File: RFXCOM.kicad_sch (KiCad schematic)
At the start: 5 parts

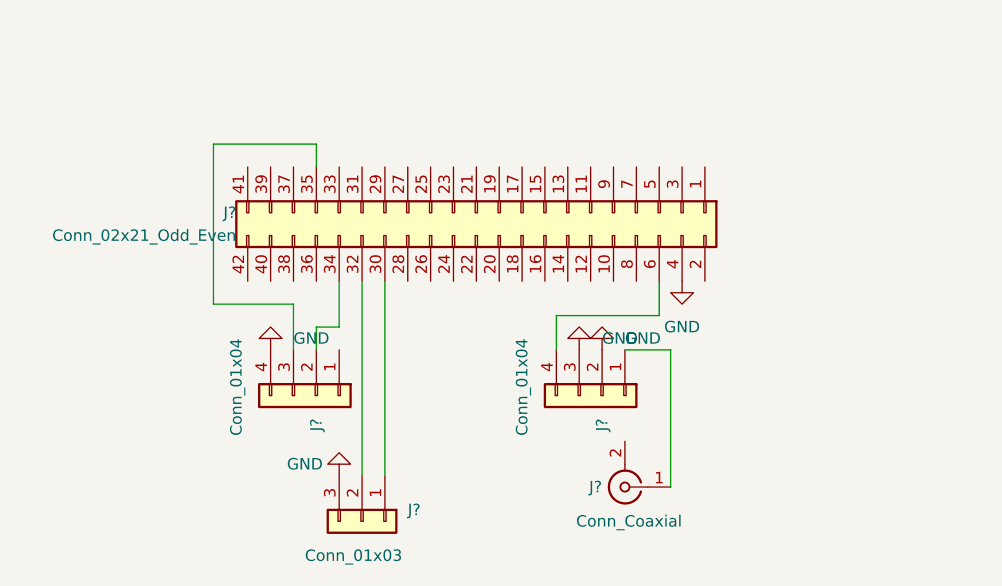
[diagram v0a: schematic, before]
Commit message: Rework the schematics a bit with labels. Add a RXB6 footprint. Also add a .gitignore
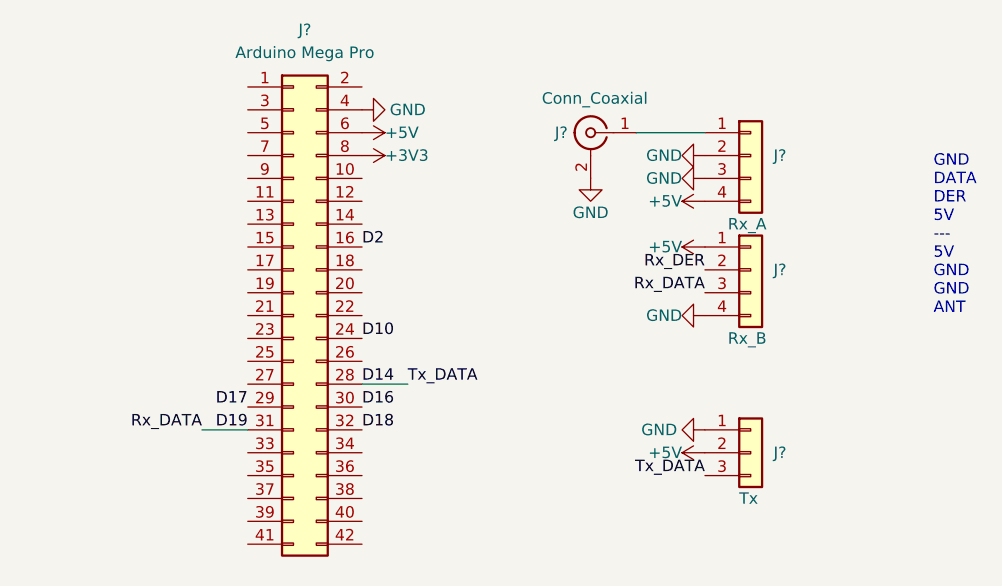
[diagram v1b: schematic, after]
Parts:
- removed J?: Conn_01x04, symbol Connector_Generic:Conn_01x04
- added J?: Rx_B, symbol Connector_Generic:Conn_01x04
- J?: value Conn_01x04 -> Rx_A
- J?: value Conn_01x03 -> Tx
- J?: value Conn_02x21_Odd_Even -> Arduino Mega Pro
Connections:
- net GND: now also J?.1 (Pin_1), J?.2 (Ext), J?.4 (Pin_4); no longer J?.3 (Pin_3)
- net +5V: now reaches J?.4 (Pin_4), J?.6 (Pin_6)
- net +5V: now also J?.2 (Pin_2), J?.1 (Pin_1)
- net D16: now reaches J?.30 (Pin_30)
- net D16: no longer J?.1 (Pin_1)
- net D18: now reaches J?.32 (Pin_32)
- net D18: no longer J?.2 (Pin_2)
- net D2: now reaches J?.16 (Pin_16)
- net D10: now reaches J?.24 (Pin_24)
- net D14: now reaches J?.28 (Pin_28)
- net D14: now also J?.3 (Pin_3)
- net D17: now reaches J?.29 (Pin_29)
- net D19: now reaches J?.31 (Pin_31)
- net D19: now also J?.3 (Pin_3)
- net +3V3: now reaches J?.8 (Pin_8)
- new net Rx_DER: J?.2 (Pin_2)
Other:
- note added: "GND DATA DER 5V --- 5V GND GND ANT"
- moved on the sheet: J?

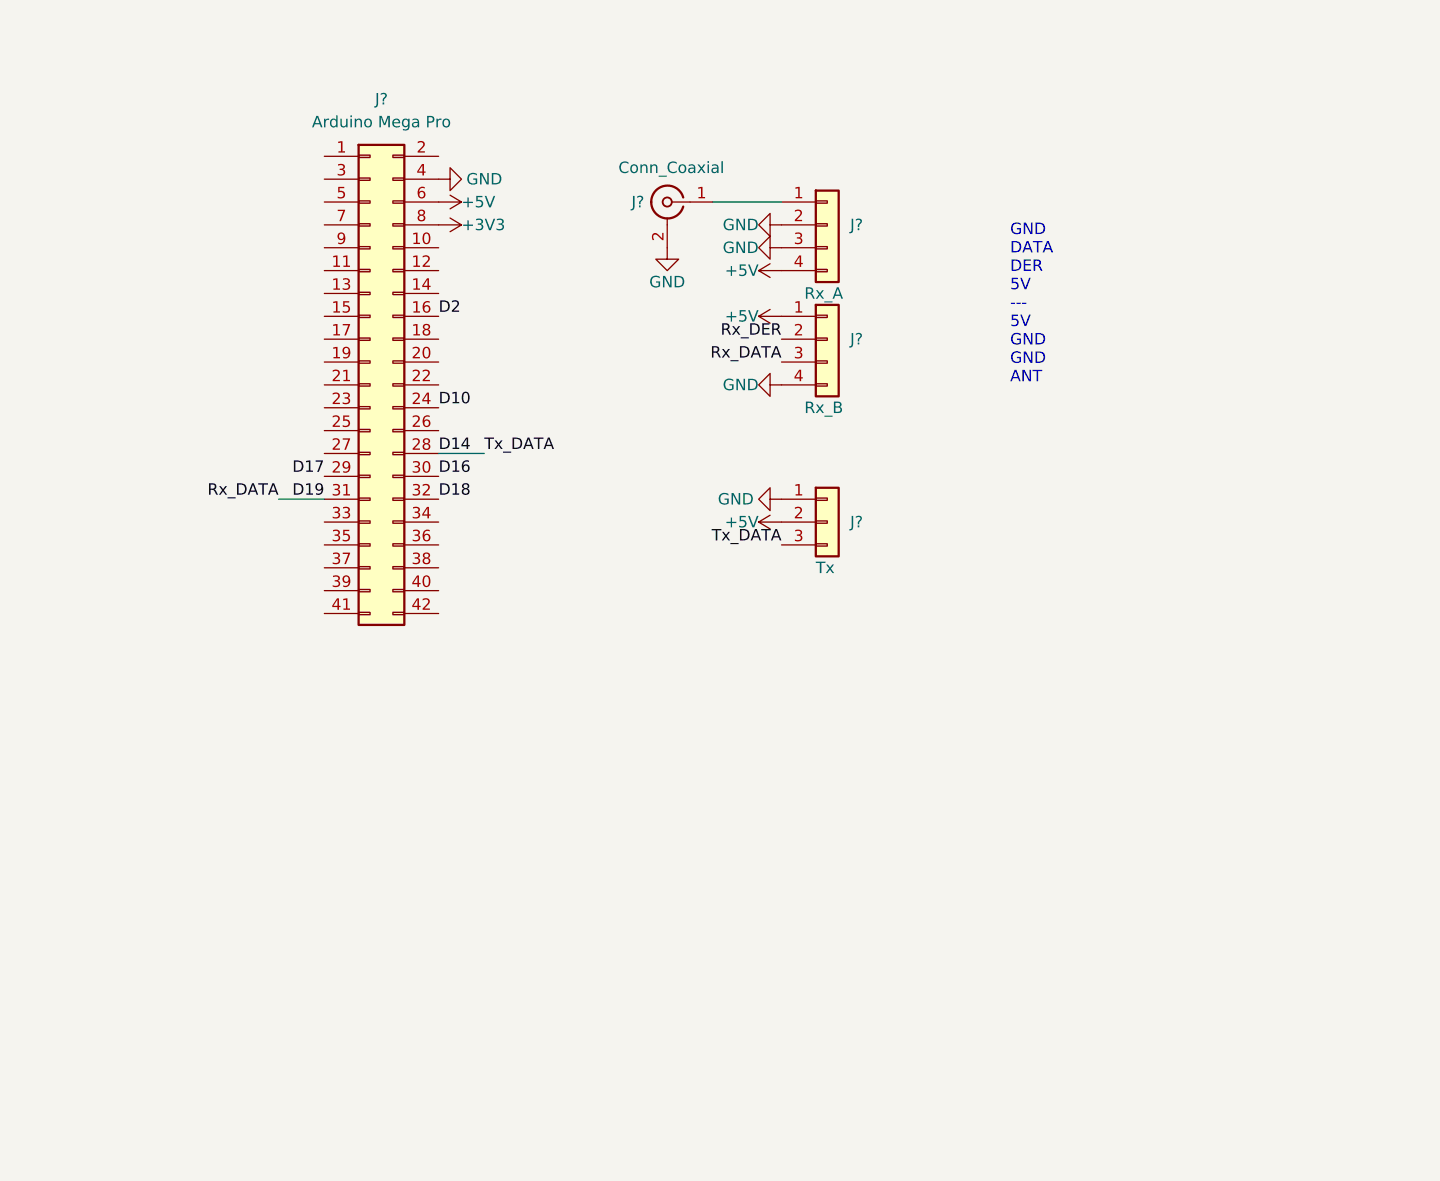
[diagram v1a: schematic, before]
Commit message: New pcb on arduino mega pro, smoothed tracks, 2 antennas
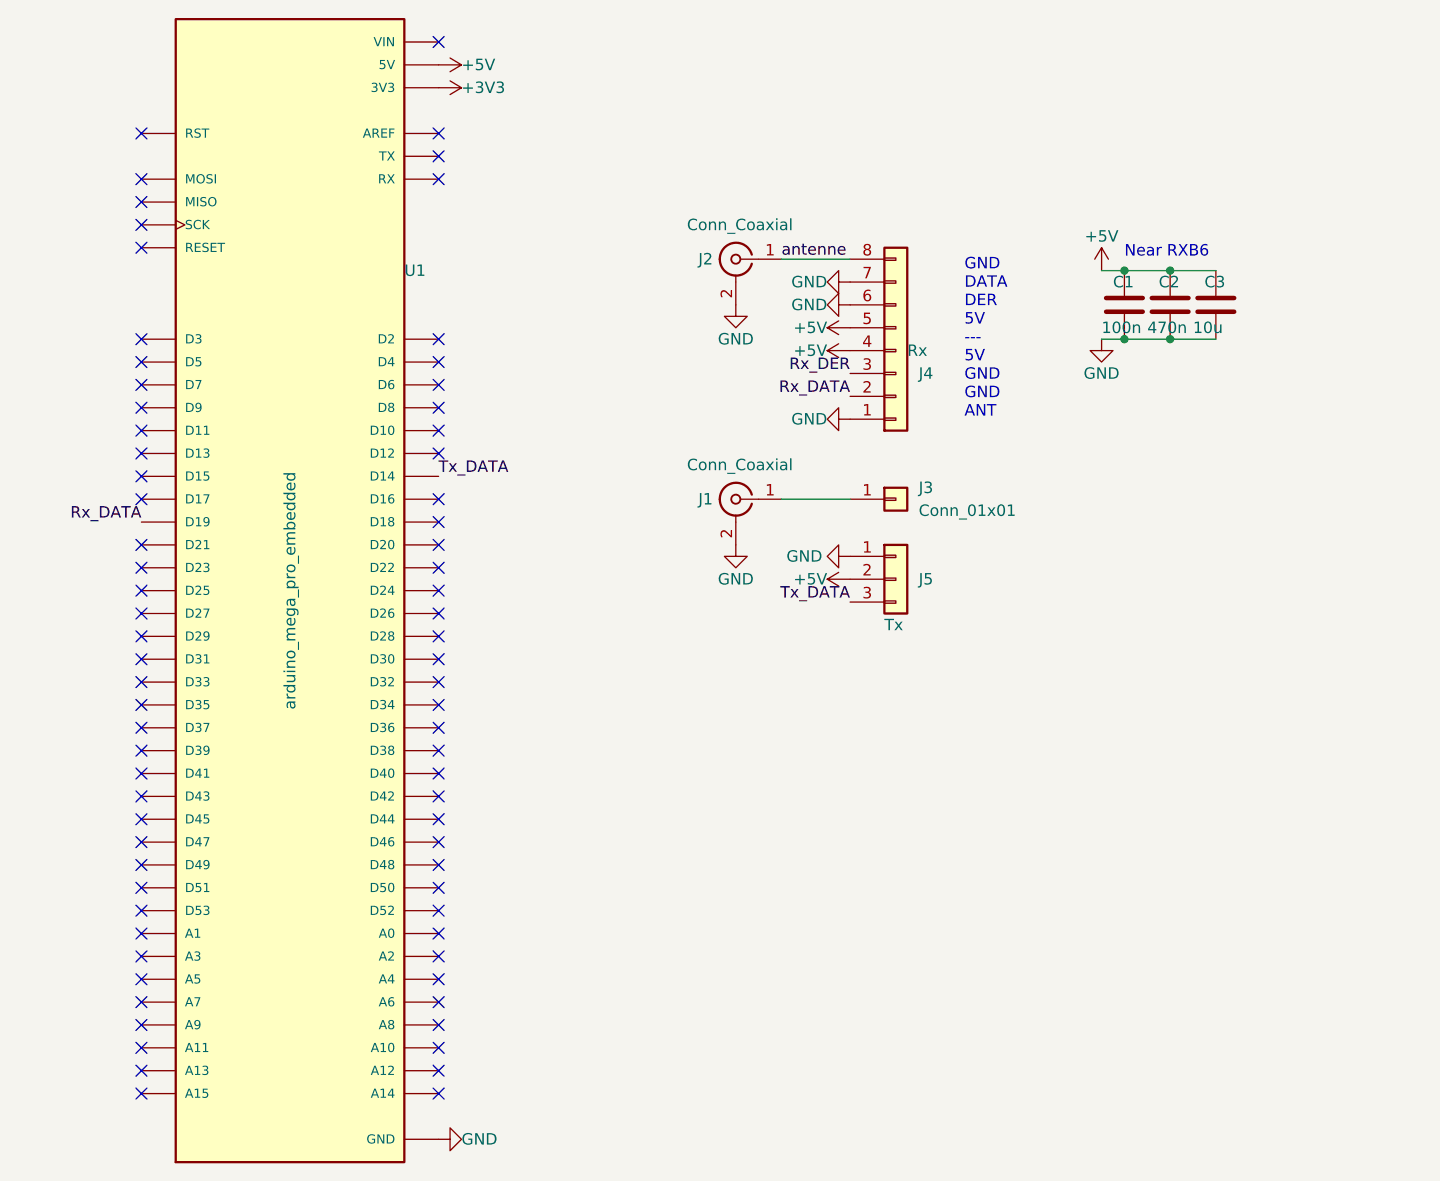
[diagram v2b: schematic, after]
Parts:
- removed J?: Rx_A, symbol Connector_Generic:Conn_01x04
- removed J?: Arduino Mega Pro, symbol Connector_Generic:Conn_02x21_Odd_Even
- added C1: 100n, Capacitor_SMD:C_0805_2012Metric_Pad1.18x1.45mm_HandSolder, symbol Device:C
- added C2: 470n, Capacitor_SMD:C_0805_2012Metric_Pad1.18x1.45mm_HandSolder, symbol Device:C
- added C3: 10u, Capacitor_SMD:C_0805_2012Metric_Pad1.18x1.45mm_HandSolder, symbol Device:C
- added J1: Conn_Coaxial, Connector_Coaxial:SMA_Amphenol_901-144_Vertical, symbol Connector:Conn_Coaxial
- added J3: Conn_01x01, Connector_PinHeader_2.54mm:PinHeader_1x01_P2.54mm_Vertical, symbol Connector_Generic:Conn_01x01
- added U1: arduino_mega_pro_embedded, rf_components:arduino_mega_pro_embedded, symbol arduino_mega_pro_embedded:arduino_mega_pro_embedded
- J2: renamed from J?; footprint (none) -> Connector_Coaxial:SMA_Amphenol_901-144_Vertical
- J4: renamed from J?; value Rx_B -> Rx; footprint (none) -> rf_components:RXB6; symbol Connector_Generic:Conn_01x04 -> Connector_Generic:Conn_01x08
- J5: renamed from J?; footprint (none) -> Connector_PinHeader_2.54mm:PinHeader_1x03_P2.54mm_Vertical
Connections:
- net D19 is gone; now on net Rx_DER: J4.3 (Pin_3)
- net +3V3: now also U1.3V3_1 (3V3), U1.3V3_2 (3V3)
- net +5V: now also J4.4 (Pin_4), J4.5 (Pin_5), C1.1, C2.1, C3.1, U1.5V_1 (5V), U1.5V_2 (5V), U1.5V_3 (5V); no longer J4.1 (Pin_1)
- net GND: now also J4.1 (Pin_1), J4.6 (Pin_6), J4.7 (Pin_7), C1.2, C2.2, C3.2, J1.2 (Ext), U1.GND_1 (GND), U1.GND_2 (GND), U1.GND_3 (GND); no longer J4.4 (Pin_4)
- net Rx_DER: no longer J4.2 (Pin_2)
- net antenne: now reaches J2.1 (In)
- net antenne: now also J4.8 (Pin_8)
- net D14 renamed Tx_DATA
- net Tx_DATA: now also U1.D14
- new net: J1.1 (In), J3.1 (Pin_1)
- new net: U1.VIN_1 (VIN), U1.VIN_2 (VIN)
- new net Rx_DATA: J4.2 (Pin_2), U1.D19
- no-connect marks 0 -> 75
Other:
- note added: "Near RXB6"
- moved on the sheet: J2, J5

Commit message: stm32 based pcb
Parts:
- removed J3: Conn_01x01, Connector_PinHeader_2.54mm:PinHeader_1x01_P2.54mm_Vertical, symbol Connector_Generic:Conn_01x01
- removed U1: arduino_mega_pro_embedded, rf_components:arduino_mega_pro_embedded, symbol arduino_mega_pro_embedded:arduino_mega_pro_embedded
- added C10: 1u, Capacitor_SMD:C_0603_1608Metric_Pad1.08x0.95mm_HandSolder, symbol Device:C
- added C11: 10n, Capacitor_SMD:C_0603_1608Metric_Pad1.08x0.95mm_HandSolder, symbol Device:C
- added C4: 4u7, Capacitor_SMD:C_0805_2012Metric_Pad1.18x1.45mm_HandSolder, symbol Device:C
- added C5, C6: 10p, Capacitor_SMD:C_0603_1608Metric_Pad1.08x0.95mm_HandSolder, symbol Device:C_Small
- added C7, C9: 100n, Capacitor_SMD:C_0603_1608Metric_Pad1.08x0.95mm_HandSolder, symbol Device:C
- added C8: 100n, Capacitor_SMD:C_0603_1608Metric_Pad1.08x0.95mm_HandSolder, symbol Device:C_Small
- added D1: LED_AGRB, LED_SMD:LED_RGB_Wuerth-PLCC4_3.2x2.8mm_150141M173100, symbol Device:LED_AGRB
- added J3: SWD_Connector, Connector_PinHeader_2.54mm:PinHeader_1x06_P2.54mm_Vertical, symbol Connector_Generic:Conn_01x06
- added J7: SWD, Connector_PinHeader_1.27mm:PinHeader_2x03_P1.27mm_Vertical_SMD, symbol Connector_Generic:Conn_02x03_Odd_Even
- added R3: 130, Resistor_SMD:R_0805_2012Metric_Pad1.20x1.40mm_HandSolder, symbol Device:R
- added R4, R5: 30, Resistor_SMD:R_0805_2012Metric_Pad1.20x1.40mm_HandSolder, symbol Device:R
- added U1: STM32L412KBTx, Package_DFN_QFN:QFN-32-1EP_5x5mm_P0.5mm_EP3.45x3.45mm, symbol stm32l412:STM32L412KBTx
- added Y1: 16M, Crystal:Crystal_SMD_Abracon_ABM8G-4Pin_3.2x2.5mm, symbol Device:Crystal_GND24
- C2: Price (none) -> 0.1
- C3: Price (none) -> 0.19
- J1: value Conn_Coaxial -> TX Antenna; MPN (none) -> 901-144-8RFX; Price (none) -> 4.65
- J2: value Conn_Coaxial -> RX Antenna; MPN (none) -> 901-144-8RFX; Price (none) -> 4.65
- J4: MPN (none) -> RXB6
- J5: footprint Connector_PinHeader_2.54mm:PinHeader_1x03_P2.54mm_Vertical -> rf_components:XKFST_Horizontal; symbol Connector_Generic:Conn_01x03 -> Connector_Generic:Conn_01x04; MPN (none) -> XD-FST FS1000A
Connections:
- net GND: now also C10.2, C11.2, C4.2, C5.1, C6.1, C7.2, C8.1, C9.2, J3.3 (Pin_3), J7.5 (Pin_5), R3.2, U1.16 (VSS), U1.32 (VSS), Y1.2, Y1.4
- net Rx_DATA: now also U1.9 (PA3)
- net Rx_DER: now also U1.10 (PA4)
- net Tx_DATA: now also U1.8 (PA2)
- net at J1.1 (In): now also J5.4 (Pin_4)
- new net: D1.2 (GK), R4.1
- new net: R4.2, U1.29 (PB6)
- new net: D1.4 (BK), R5.1
- new net: R5.2, U1.30 (PB7)
- new net: C6.2, U1.3 (PC15), Y1.1
- new net: C5.2, U1.2 (PC14), Y1.3
- new net: D1.3 (RK), R3.1
- new net +3.3V: C4.1, C7.1, C9.1, D1.1 (A), J7.1 (Pin_1), U1.1 (VDD), U1.17 (VDD)
- new net +3.3VA: C10.1, C11.1, U1.5 (VDDA)
- new net BOOT0: U1.31 (PH3)
- new net SWCLK: J3.2 (Pin_2), J7.4 (Pin_4), U1.24 (PA14)
- new net SWDIO: J3.4 (Pin_4), J7.2 (Pin_2), U1.23 (PA13)
- new net SWO: J3.6 (Pin_6), J7.6 (Pin_6), U1.26 (PB3)
- new net USB_D+: U1.22 (PA12)
- new net USB_D-: U1.21 (PA11)
- new net ~{RST}: C8.2, J3.5 (Pin_5), J7.3 (Pin_3), U1.4 (NRST)
- no-connect marks 75 -> 14
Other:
- added sheet USB & Power Supply (usb.kicad_sch)
- note added: "ANT GND GND 5V --- 5V DER DATA GND"
- note added: "Near STM32"
- note removed: "GND DATA DER 5V --- 5V GND GND ANT"
- moved on the sheet: C1, C2, C3, J1, J2, J4
